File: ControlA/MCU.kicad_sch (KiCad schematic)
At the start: 38 parts

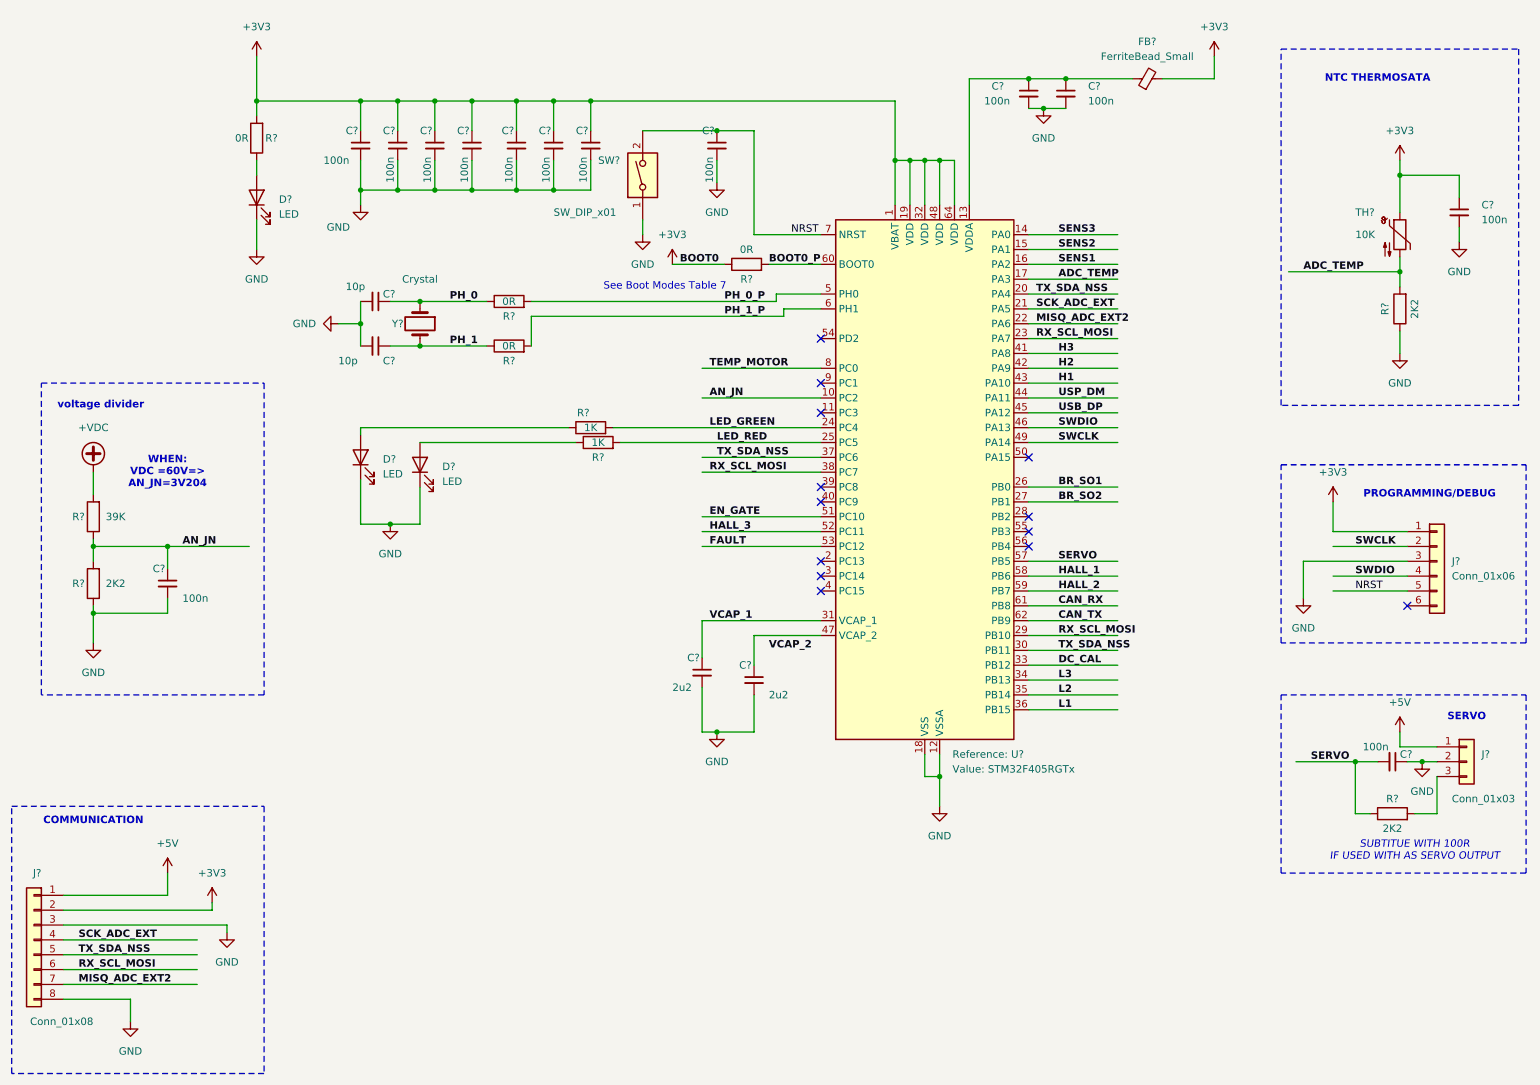
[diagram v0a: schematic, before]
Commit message: final shema symbole
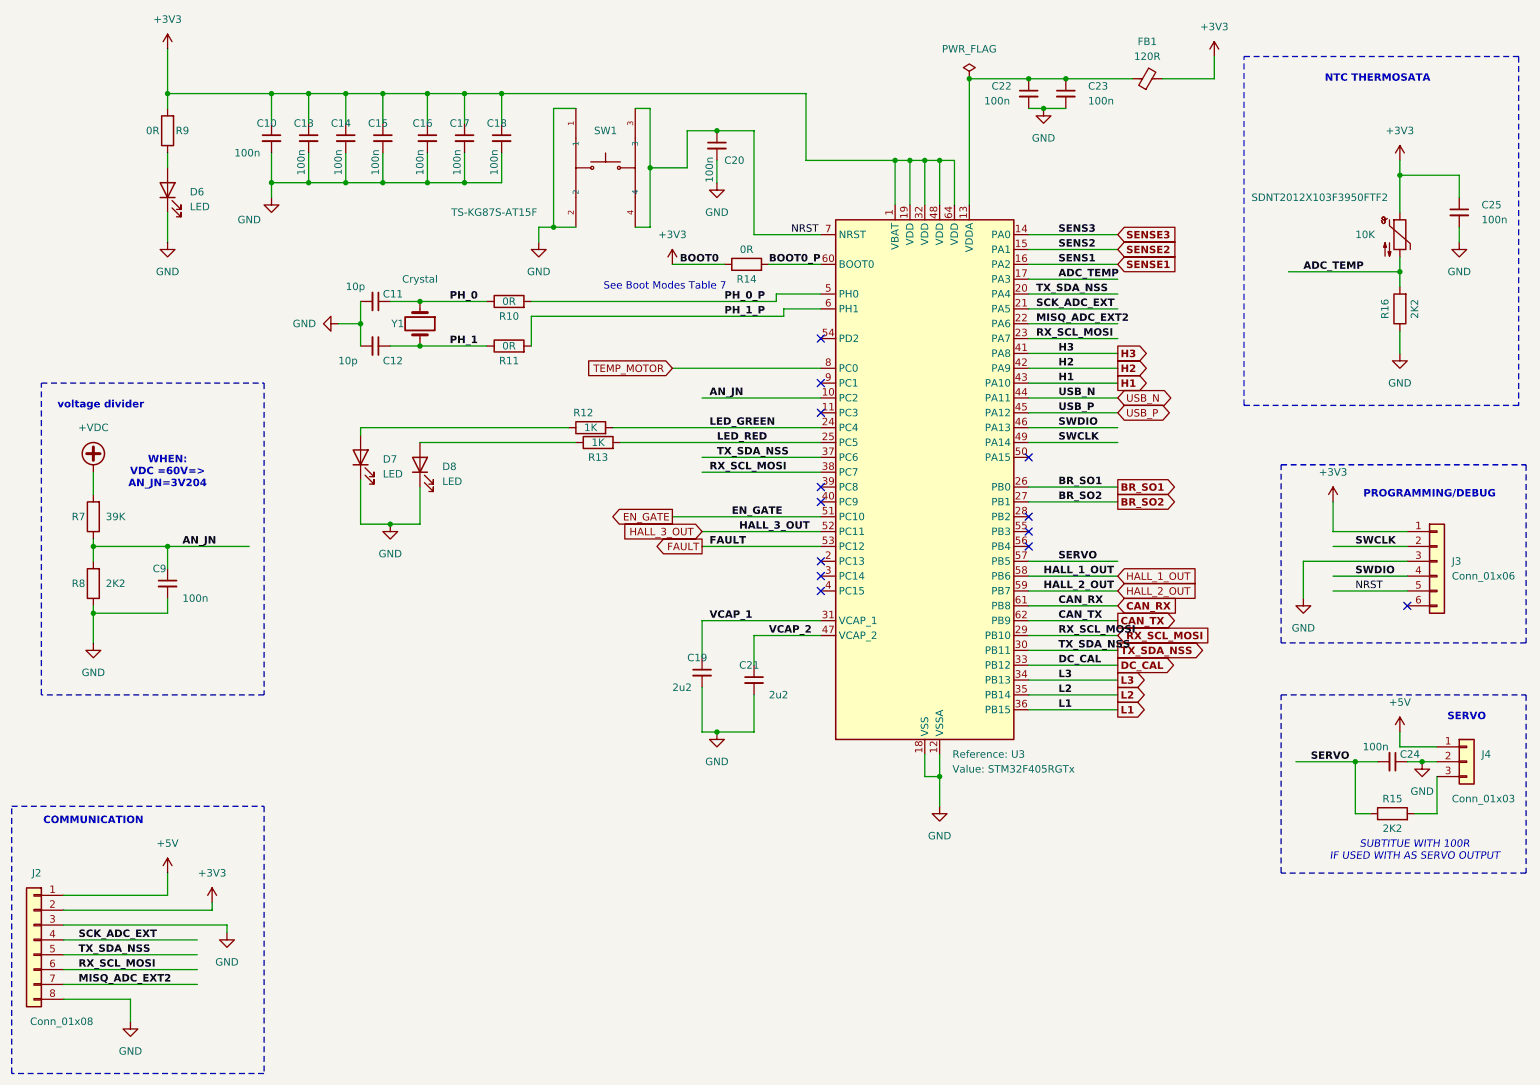
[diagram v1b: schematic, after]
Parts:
- removed SW?: SW_DIP_x01, symbol Switch:SW_DIP_x01
- added SW1: TS-KG87S-AT15F, footprint:SW-SMD_4P-L5.2-W5.2-P3.70-LS6.4, symbol TS-KG87S-AT15F:TS-KG87S-AT15F
- C10, C11, C12, C9: renamed from C?; footprint (none) -> Capacitor_SMD:C_0805_2012Metric
- C13, C14, C15, C16, C17, C18, C20, C22, C23, C24, C25: renamed from C?; footprint (none) -> Capacitor_SMD:C_0402_1005Metric
- C19, C21: renamed from C?; footprint (none) -> Capacitor_SMD:C_0603_1608Metric
- D6, D7, D8: renamed from D?; footprint (none) -> footprint:LED0805-R-RD
- FB1: renamed from FB?; value FerriteBead_Small -> 120R; footprint (none) -> footprint:L0603
- J2: renamed from J?; footprint (none) -> Connector_PinHeader_1.00mm:PinHeader_1x08_P1.00mm_Vertical
- J3: renamed from J?; footprint (none) -> Connector_PinHeader_1.00mm:PinHeader_1x06_P1.00mm_Vertical
- J4: renamed from J?; footprint (none) -> Connector_PinHeader_1.00mm:PinHeader_1x03_P1.00mm_Vertical
- R10, R11, R12, R13, R14, R15, R16, R7, R8, R9: renamed from R?; footprint (none) -> Resistor_SMD:R_0805_2012Metric
- SDNT2012X103F3950FTF2: renamed from TH?; footprint (none) -> Resistor_SMD:R_0805_2012Metric
- Y1: renamed from Y?; footprint (none) -> Crystal:Crystal_SMD_5032-2Pin_5.0x3.2mm
- gave numbers to parts that had none: 1
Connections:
- net GND: now also SW1.1, SW1.2
- net NRST: now also SW1.3, SW1.4
- net VCAP_2: now also C21.1, U3.47 (VCAP_2)
- net HALL_1 renamed HALL_1_OUT
- net HALL_2 renamed HALL_2_OUT
- net HALL_3 renamed HALL_3_OUT
- net SENS1 renamed SENSE1
- net SENS2 renamed SENSE2
- net SENS3 renamed SENSE3
- net USB_DP renamed USB_P
- net USP_DM renamed USB_N
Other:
- moved on the sheet: C10, C13, C14, C15, C16, C17, C18, D6, R9

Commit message: CHANGE V11
change v1
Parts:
- C10, C11, C12, C9: footprint Capacitor_SMD:C_0805_2012Metric -> Capacitor_SMD:C_0603_1608Metric
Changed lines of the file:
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@@
 			)
 		)
-		(property "Footprint" "Capacitor_SMD:C_0805_2012Metric"
+		(property "Footprint" "Capacitor_SMD:C_0603_1608Metric"
 			(at 44.45 109.22 0)
 			(effects
@@
 			)
 		)
-		(property "Footprint" "Capacitor_SMD:C_0805_2012Metric"
+		(property "Footprint" "Capacitor_SMD:C_0603_1608Metric"
 			(at 80.01 68.58 0)
 			(effects
@@
 			)
 		)
-		(property "Footprint" "Capacitor_SMD:C_0805_2012Metric"
+		(property "Footprint" "Capacitor_SMD:C_0603_1608Metric"
 			(at 80.01 60.96 0)
 			(effects
@@
 			)
 		)
-		(property "Footprint" "Capacitor_SMD:C_0805_2012Metric"
+		(property "Footprint" "Capacitor_SMD:C_0603_1608Metric"
 			(at 62.23 33.02 0)
 			(effects

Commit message: layout
layout mcu
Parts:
- R10, R11: footprint Resistor_SMD:R_0805_2012Metric -> Resistor_SMD:R_0402_1005Metric
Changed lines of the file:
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@@
 			)
 		)
-		(property "Footprint" "Resistor_SMD:R_0805_2012Metric"
+		(property "Footprint" "Resistor_SMD:R_0402_1005Metric"
 			(at 102.87 62.738 90)
 			(effects
@@
 			)
 		)
-		(property "Footprint" "Resistor_SMD:R_0805_2012Metric"
+		(property "Footprint" "Resistor_SMD:R_0402_1005Metric"
 			(at 102.87 70.358 90)
 			(effects

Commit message: change in shama
change schema and lyout
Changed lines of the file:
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@@
 	)
 	(junction
-		(at 138.43 31.75)
+		(at 63.5 40.64)
 		(diameter 0)
 		(color 0 0 0 0)
 	)
 	(junction
-		(at 255.27 55.88)
+		(at 138.43 31.75)
 		(diameter 0)
 		(color 0 0 0 0)
 	)
 	(junction
-		(at 44.45 102.87)
+		(at 255.27 55.88)
 		(diameter 0)
 		(color 0 0 0 0)
 	)
 	(junction
-		(at 62.23 40.64)
+		(at 44.45 102.87)
 		(diameter 0)
 		(color 0 0 0 0)
@@
 	(wire
 		(pts
-			(xy 62.23 40.64) (xy 68.58 40.64)
+			(xy 62.23 40.64) (xy 63.5 40.64)
 		)
 		(stroke
@@
 	(wire
 		(pts
-			(xy 247.65 148.59) (xy 247.65 139.7)
+			(xy 68.58 40.64) (xy 74.93 40.64)
 		)
 		(stroke
@@
 	(wire
 		(pts
-			(xy 44.45 50.8) (xy 44.45 45.72)
+			(xy 247.65 148.59) (xy 247.65 139.7)
 		)
 		(stroke
@@
 	(wire
 		(pts
-			(xy 255.27 69.85) (xy 255.27 66.04)
+			(xy 44.45 50.8) (xy 44.45 45.72)
 		)
 		(stroke
@@
 	(wire
 		(pts
-			(xy 31.75 90.17) (xy 31.75 93.98)
+			(xy 255.27 69.85) (xy 255.27 66.04)
 		)
 		(stroke
@@
 	(wire
 		(pts
-			(xy 191.77 82.55) (xy 207.01 82.55)
+			(xy 31.75 90.17) (xy 31.75 93.98)
 		)
 		(stroke
@@
 	(wire
 		(pts
-			(xy 149.86 63.5) (xy 149.86 62.23)
+			(xy 191.77 82.55) (xy 207.01 82.55)
 		)
 		(stroke
@@
 	(wire
 		(pts
-			(xy 62.23 40.64) (xy 62.23 43.18)
+			(xy 149.86 63.5) (xy 149.86 62.23)
 		)
 		(stroke
@@
 	(wire
 		(pts
-			(xy 68.58 40.64) (xy 74.93 40.64)
-		)
-		(stroke
-			(width 0)
-			(type default)
-		)
-	)
-	(wire
-		(pts
 			(xy 176.53 36.83) (xy 176.53 44.45)
 		)
@@
 	(wire
 		(pts
+			(xy 63.5 40.64) (xy 63.5 53.34)
+		)
+		(stroke
+			(width 0)
+			(type default)
+		)
+	)
+	(wire
+		(pts
 			(xy 81.28 25.4) (xy 88.9 25.4)
 		)
@@
 	(wire
 		(pts
+			(xy 63.5 40.64) (xy 68.58 40.64)
+		)
+		(stroke
+			(width 0)
+			(type default)
+		)
+	)
+	(wire
+		(pts
 			(xy 68.58 35.56) (xy 68.58 40.64)
 		)
@@
 	(wire
 		(pts
-			(xy 62.23 25.4) (xy 62.23 30.48)
+			(xy 74.93 40.64) (xy 81.28 40.64)
 		)
 		(stroke
@@
 	(wire
 		(pts
-			(xy 74.93 40.64) (xy 81.28 40.64)
+			(xy 62.23 25.4) (xy 62.23 30.48)
 		)
 		(stroke
@@
 	(symbol
 		(lib_id "power:GND")
-		(at 62.23 43.18 0)
+		(at 265.43 50.8 0)
 		(unit 1)
 		(exclude_from_sim no)
@@
 		(on_board yes)
 		(dnp no)
-		(property "Reference" "#PWR02"
-			(at 62.23 49.53 0)
+		(fields_autoplaced yes)
+		(property "Reference" "#PWR019"
+			(at 265.43 57.15 0)
 			(effects
 				(font
@@
 		)
 		(property "Value" "GND"
-			(at 58.42 46.99 0)
+			(at 265.43 55.88 0)
 			(effects
 				(font
@@
 		)
 		(property "Footprint" ""
-			(at 62.23 43.18 0)
+			(at 265.43 50.8 0)
 			(effects
 				(font
@@
 		)
 		(property "Datasheet" ""
-			(at 62.23 43.18 0)
+			(at 265.43 50.8 0)
 			(effects
 				(font
@@
 		)
 		(property "Description" "Power symbol creates a global label with name \"GND\" , ground"
-			(at 62.23 43.18 0)
+			(at 265.43 50.8 0)
 			(effects
 				(font
@@
 			(project "ControlA"
 				(path "/28f77b05-53a5-4f29-9b4d-d18dbf030970/a6064041-ecb6-4b5c-a3b1-f3c20e6d8583"
-					(reference "#PWR02")
+					(reference "#PWR019")
 					(unit 1)
 				)
@@
 	)
 	(symbol
-		(lib_id "power:GND")
-		(at 265.43 50.8 0)
+		(lib_id "Device:C_Small")
+		(at 81.28 33.02 0)
 		(unit 1)
 		(exclude_from_sim no)
@@
 		(on_board yes)
 		(dnp no)
-		(fields_autoplaced yes)
-		(property "Reference" "#PWR019"
-			(at 265.43 57.15 0)
+		(property "Reference" "C15"
+			(at 78.74 30.48 0)
 			(effects
 				(font
 					(size 1.27 1.27)
 				)
-				(hide yes)
+				(justify left)
 			)
 		)
-		(property "Value" "GND"
-			(at 265.43 55.88 0)
+		(property "Value" "100n"
+			(at 80.01 39.37 90)
 			(effects
 				(font
 					(size 1.27 1.27)
 				)
+				(justify left)
 			)
 		)
-		(property "Footprint" ""
-			(at 265.43 50.8 0)
+		(property "Footprint" "Capacitor_SMD:C_0402_1005Metric"
+			(at 81.28 33.02 0)
 			(effects
 				(font
@@
 			)
 		)
-		(property "Datasheet" ""
-			(at 265.43 50.8 0)
+		(property "Datasheet" "~"
+			(at 81.28 33.02 0)
 			(effects
 				(font
@@
 			)
 		)
-		(property "Description" "Power symbol creates a global label with name \"GND\" , ground"
-			(at 265.43 50.8 0)
+		(property "Description" "Unpolarized capacitor, small symbol"
+			(at 81.28 33.02 0)
 			(effects
 				(font
@@
 			)
 		)
+		(pin "2"
+		)
 		(pin "1"
 		)
@@
 			(project "ControlA"
 				(path "/28f77b05-53a5-4f29-9b4d-d18dbf030970/a6064041-ecb6-4b5c-a3b1-f3c20e6d8583"
-					(reference "#PWR019")
+					(reference "C15")
 					(unit 1)
 				)
@@
 	(symbol
 		(lib_id "Device:C_Small")
-		(at 81.28 33.02 0)
+		(at 135.89 124.46 0)
 		(unit 1)
 		(exclude_from_sim no)
@@
 		(on_board yes)
 		(dnp no)
-		(property "Reference" "C15"
-			(at 78.74 30.48 0)
+		(property "Reference" "C19"
+			(at 133.35 121.92 0)
 			(effects
 				(font
@@
 			)
 		)
-		(property "Value" "100n"
-			(at 80.01 39.37 90)
+		(property "Value" "2u2"
+			(at 130.81 127 0)
 			(effects
 				(font
@@
 			)
 		)
-		(property "Footprint" "Capacitor_SMD:C_0402_1005Metric"
-			(at 81.28 33.02 0)
+		(property "Footprint" "Capacitor_SMD:C_0603_1608Metric"
+			(at 135.89 124.46 0)
 			(effects
 				(font
@@
 		)
 		(property "Datasheet" "~"
-			(at 81.28 33.02 0)
+			(at 135.89 124.46 0)
 			(effects
 				(font
@@
 		)
 		(property "Description" "Unpolarized capacitor, small symbol"
-			(at 81.28 33.02 0)
+			(at 135.89 124.46 0)
 			(effects
 				(font
@@
 			(project "ControlA"
 				(path "/28f77b05-53a5-4f29-9b4d-d18dbf030970/a6064041-ecb6-4b5c-a3b1-f3c20e6d8583"
-					(reference "C15")
+					(reference "C19")
 					(unit 1)
 				)
@@
 	(symbol
 		(lib_id "Device:C_Small")
-		(at 135.89 124.46 0)
+		(at 62.23 33.02 0)
 		(unit 1)
 		(exclude_from_sim no)
@@
 		(on_board yes)
 		(dnp no)
-		(property "Reference" "C19"
-			(at 133.35 121.92 0)
+		(property "Reference" "C10"
+			(at 59.69 30.48 0)
 			(effects
 				(font
@@
 			)
 		)
-		(property "Value" "2u2"
-			(at 130.81 127 0)
+		(property "Value" "100n"
+			(at 55.88 35.56 0)
 			(effects
 				(font
@@
 		)
 		(property "Footprint" "Capacitor_SMD:C_0603_1608Metric"
-			(at 135.89 124.46 0)
+			(at 62.23 33.02 0)
 			(effects
 				(font
@@
 		)
 		(property "Datasheet" "~"
-			(at 135.89 124.46 0)
+			(at 62.23 33.02 0)
 			(effects
 				(font
@@
 		)
 		(property "Description" "Unpolarized capacitor, small symbol"
-			(at 135.89 124.46 0)
+			(at 62.23 33.02 0)
 			(effects
 				(font
@@
 			(project "ControlA"
 				(path "/28f77b05-53a5-4f29-9b4d-d18dbf030970/a6064041-ecb6-4b5c-a3b1-f3c20e6d8583"
-					(reference "C19")
+					(reference "C10")
 					(unit 1)
 				)
@@
 	)
 	(symbol
-		(lib_id "Device:C_Small")
-		(at 62.23 33.02 0)
+		(lib_id "power:GND")
+		(at 63.5 53.34 0)
 		(unit 1)
 		(exclude_from_sim no)
@@
 		(on_board yes)
 		(dnp no)
-		(property "Reference" "C10"
-			(at 59.69 30.48 0)
+		(fields_autoplaced yes)
+		(property "Reference" "#PWR02"
+			(at 63.5 59.69 0)
 			(effects
 				(font
 					(size 1.27 1.27)
 				)
-				(justify left)
+				(hide yes)
 			)
 		)
-		(property "Value" "100n"
-			(at 55.88 35.56 0)
+		(property "Value" "GND"
+			(at 63.5 58.42 0)
 			(effects
 				(font
 					(size 1.27 1.27)
 				)
-				(justify left)
 			)
 		)
-		(property "Footprint" "Capacitor_SMD:C_0603_1608Metric"
-			(at 62.23 33.02 0)
+		(property "Footprint" ""
+			(at 63.5 53.34 0)
 			(effects
 				(font
@@
 			)
 		)
-		(property "Datasheet" "~"
-			(at 62.23 33.02 0)
+		(property "Datasheet" ""
+			(at 63.5 53.34 0)
 			(effects
 				(font
@@
 			)
 		)
-		(property "Description" "Unpolarized capacitor, small symbol"
-			(at 62.23 33.02 0)
+		(property "Description" "Power symbol creates a global label with name \"GND\" , ground"
+			(at 63.5 53.34 0)
 			(effects
 				(font
@@
 			)
 		)
-		(pin "2"
-		)
 		(pin "1"
 		)
@@
 			(project "ControlA"
 				(path "/28f77b05-53a5-4f29-9b4d-d18dbf030970/a6064041-ecb6-4b5c-a3b1-f3c20e6d8583"
-					(reference "C10")
+					(reference "#PWR02")
 					(unit 1)
 				)
